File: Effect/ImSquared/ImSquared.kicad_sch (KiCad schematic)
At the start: 55 parts, among them J1 Conn_01x04_Pin, J2 Conn_01x03_Pin, Q1 DMMT5551, Q2 DMMT5551, Q3 DMMT5551, Q4 DMMT5551, U1 OPA1656, U2 OPA1656, U3 OPA1656

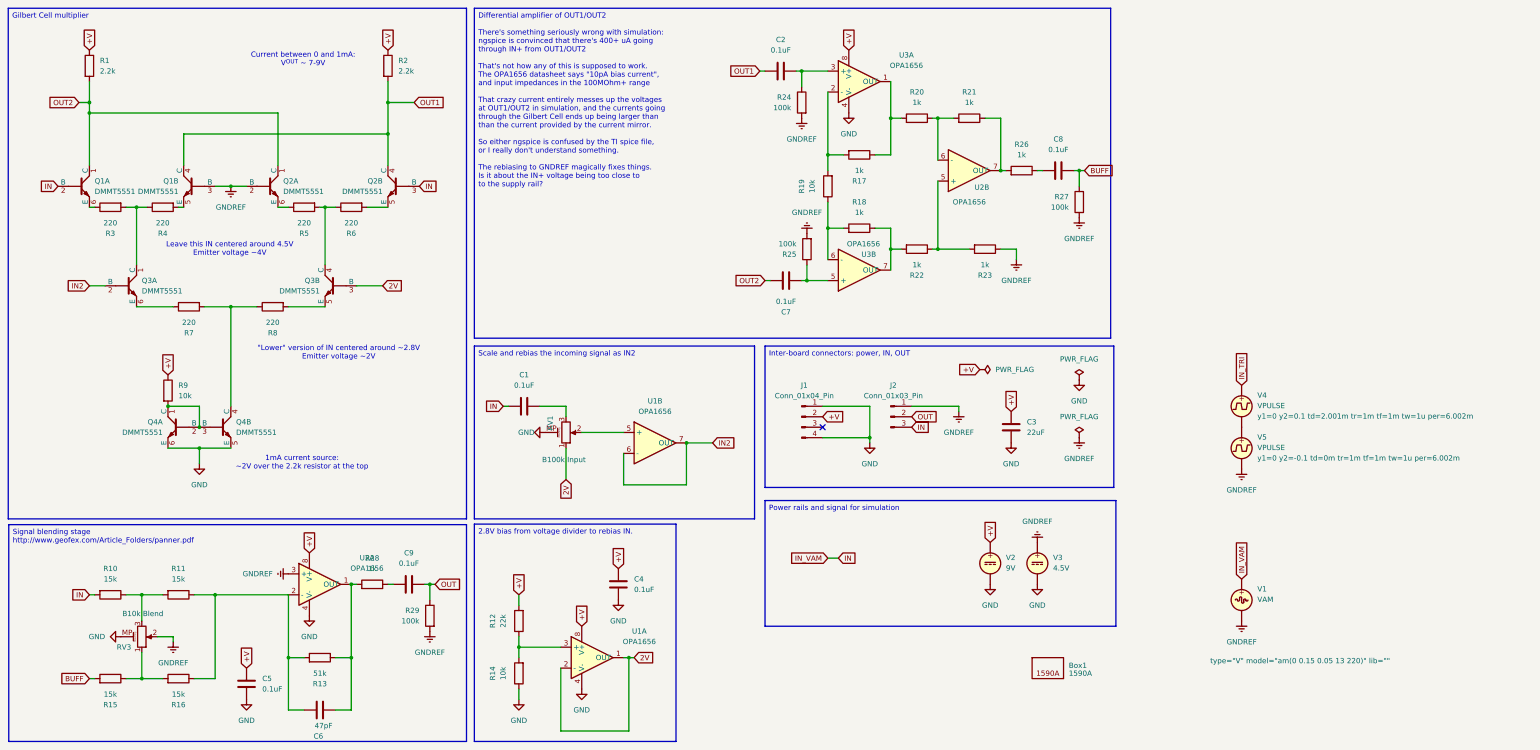
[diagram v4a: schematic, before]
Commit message: Try simulating an actual wav file input with new locally-built tooling
So this "works" in the sense that I built local copies of ngspice and
kicad and now it supports wav file input and output to simulation, and I
am trying to use some sample files to simulate what the heck it does and
sounds like.

That didn't work very well because the linear interpolation of samples
in the experimental ngspice wav branch seems quite broken, causing the
input signal to be more of a discrete staircase signal.

Which in turn then caused pretty much immediate "Timestep too small"
errors for the simulation because it's much too sensitive to not
converging, and the stepwise voltage jumps seemed to make an already
fragile situation much much worse.

I have a local hack for that ngspice sample interpolation issue that
makes the simulation mostly work, in that now I see the result on the
real signal.  I can make it even generate a result wav-file, but only if
I end up removing a lot of the surrounding circuitry, because ngspice
still ends up crapping out eventually even with my linearization fixlet.

The goal? See why the effect seems to simply not work very well on bass
guitar (although I have a suspicion that it's just the fact that the
rest of the sound path ends up filtering everything up and cleaning up
the fuzz).

I do suspect that the whole "use squaring as a octaver fuzz" is a
completely broken concept to begin with, but setting things up to use a
real signal is still a good idea.

Signed-off-by: Linus Torvalds <torvalds@linux-foundation.org>
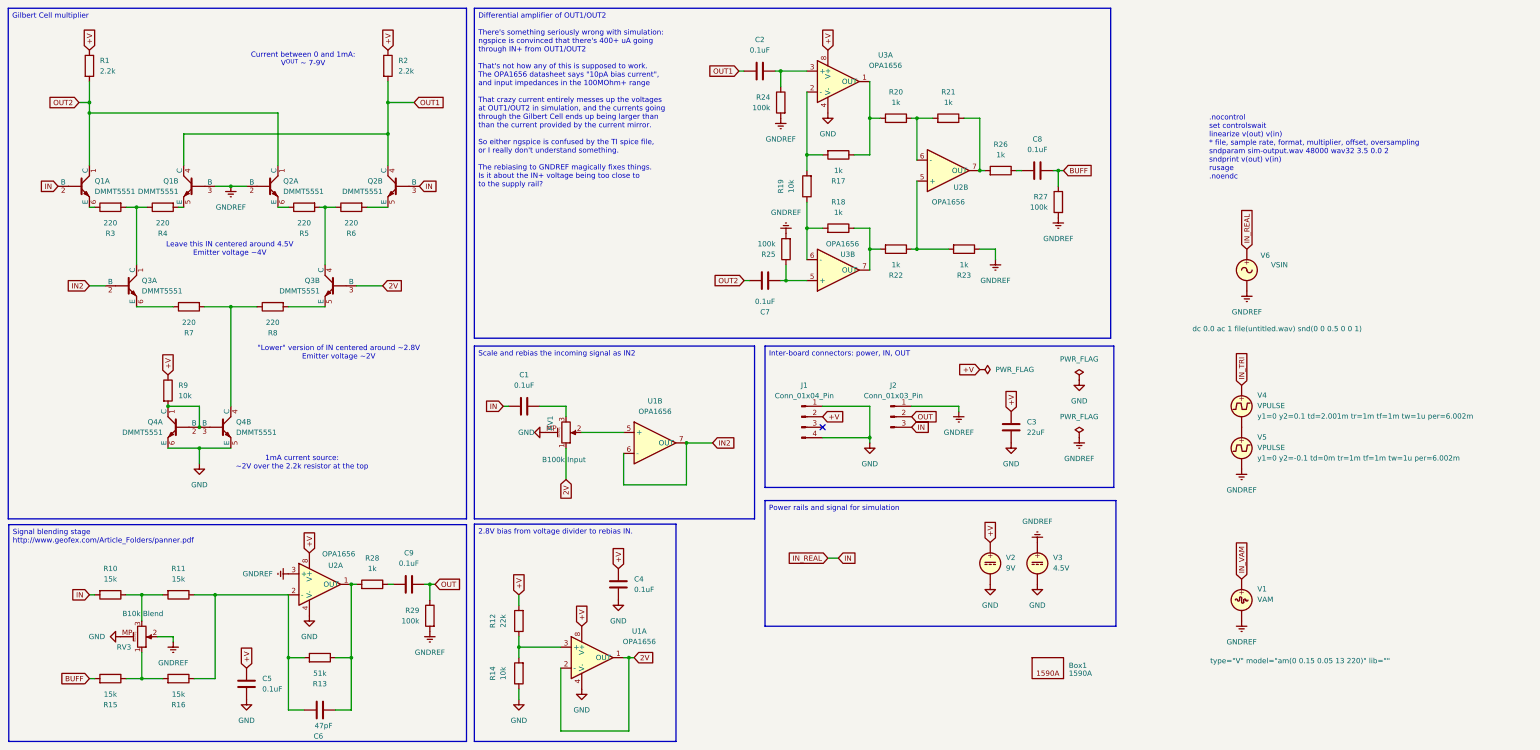
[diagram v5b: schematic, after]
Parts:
- added V6: VSIN, symbol Simulation_SPICE:VSIN
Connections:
- net GNDREF: now also V6.2
- net IN: now also V6.1; no longer V1.1
- new net IN_VAM: V1.1
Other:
- note added: ".nocontrol set controlswait linearize v(out) v(in) * file, sample rate, format, multiplier, offset, oversampling sndparam sim-output.wav 48000 wav32 3.5 0.0 2 sndprint v(out) v(in) rusage .noendc"
- moved on the sheet: C2, C7, C8, R17, R18, R19, R20, R21, R22, R23, R24, R25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

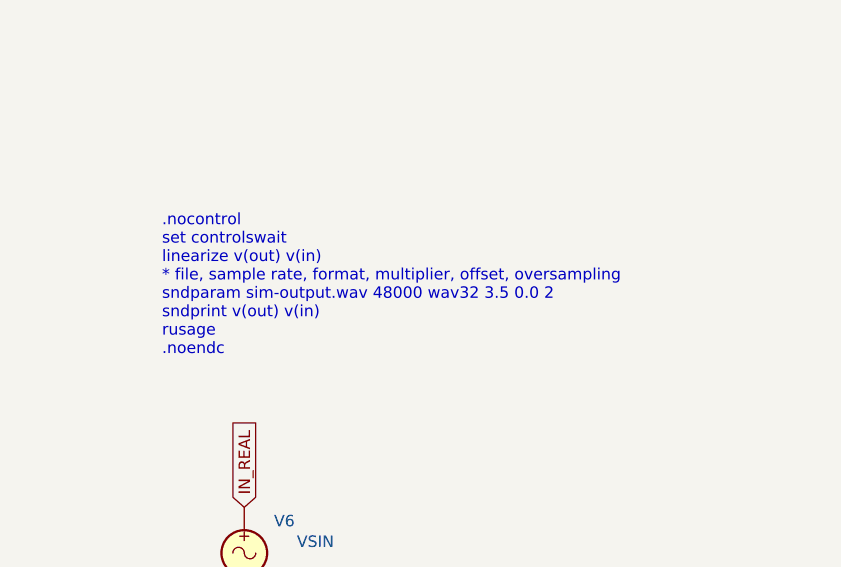
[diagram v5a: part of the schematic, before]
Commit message: Re-enable writing simulation result output wav file
Based on some hints from Holger Vogt I actually got the whole ImSquared
circuit to simulate for a full five-second sound simulation.  So now I
can hear it sounding bad without actually having hardware back.

So this enables the writeback of the sim-output.wav file, and uses the
offset parameter to get a proper signal output even at GNDREF instead of
having to re-bias the output to real ground in the circuit itself.

[ NOTE NOTE NOTE: I wasted more time than I'd like to admit on this due
  to interactions between kicad and ngspice.

  In particular, changing the parameters in the kicad text fields
  requires you to just quit and restart the whole thing for things to
  actually take effect.

  That was very confusing with me making changes to the parameters that
  didn't take effect. I'm sure I'll forget about this once more, so
  adding a big note to myself here about it. ]

It really doesn't sound great, but the circuit works, and simulation now
works too (but still needs my ngspice patch for input sample
interpolation).

The whole signal squaring approach does actually seem to work as a
octaver fuzz, but it's obviously a lot more sensitive to the input
voltage range than a plain precision rectification circuit is.

With the rectifier circuit, the output amplitude has a simple linear
relationship with the input signal, while the squaring function is
obviously non-linear.

It still might be an advantage once you mix in the original signal, with
a quiet signal giving much less distortion than a loud one.  But based
on limited testing, it ends up being pretty finicky so that "advantage"
is rather questionable.

Still, this exercise has taught me something new.  Both on the circuit
side and about ngspice.

Signed-off-by: Linus Torvalds <torvalds@linux-foundation.org>
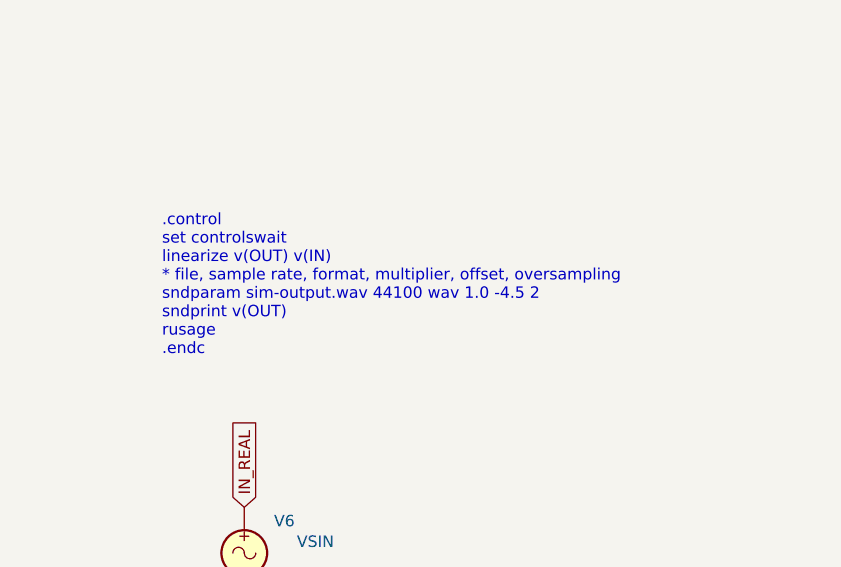
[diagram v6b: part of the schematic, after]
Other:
- note added: ".control set controlswait linearize v(OUT) v(IN) * file, sample rate, format, multiplier, offset, oversampling sndparam sim-output.wav 44100 wav 1.0 -4.5 2 sndprint v(OUT) rusage .endc"
- note removed: ".nocontrol set controlswait linearize v(out) v(in) * file, sample rate, format, multiplier, offset, oversampling sndparam sim-output.wav 48000 wav32 3.5 0.0 2 sndprint v(out) v(in) rusage .noendc"
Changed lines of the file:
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@@
 		)
 	)
-	(text ".nocontrol\nset controlswait\nlinearize v(out) v(in)\n* file, sample rate, format, multiplier, offset, oversampling\nsndparam sim-output.wav 48000 wav32 3.5 0.0 2\nsndprint v(out) v(in)\nrusage\n.noendc\n"
+	(text ".control\nset controlswait\nlinearize v(OUT) v(IN)\n* file, sample rate, format, multiplier, offset, oversampling\nsndparam sim-output.wav 44100 wav 1.0 -4.5 2\nsndprint v(OUT)\nrusage\n.endc\n"
 		(exclude_from_sim no)
 		(at 304.546 47.752 0)
@@
 	)
 	(symbol
-		(lib_id "power:GNDREF")
-		(at 115.57 165.1 0)
-		(unit 1)
-		(exclude_from_sim no)
-		(in_bom yes)
-		(on_board yes)
-		(dnp no)
-		(fields_autoplaced yes)
-		(property "Reference" "#PWR027"
-			(at 115.57 171.45 0)
-			(hide yes)
-			(effects
-				(font
-					(size 1.27 1.27)
-				)
-			)
-		)
-		(property "Value" "GNDREF"
-			(at 115.57 170.18 0)
-			(effects
-				(font
-					(size 1.27 1.27)
-				)
-			)
-		)
-		(property "Footprint" ""
-			(at 115.57 165.1 0)
-			(hide yes)
-			(effects
-				(font
-					(size 1.27 1.27)
-				)
-			)
-		)
-		(property "Datasheet" ""
-			(at 115.57 165.1 0)
-			(hide yes)
-			(effects
-				(font
-					(size 1.27 1.27)
-				)
-			)
-		)
-		(property "Description" "Power symbol creates a global label with name \"GNDREF\" , reference supply ground"
-			(at 115.57 165.1 0)
-			(hide yes)
-			(effects
-				(font
-					(size 1.27 1.27)
-				)
-			)
-		)
-		(pin "1"
-		)
-		(instances
-			(project "ImSquared"
-				(path "/9e337e0b-885b-4d2b-99a2-62cdd082c615"
-					(reference "#PWR027")
-					(unit 1)
-				)
-			)
-		)
-	)
-	(symbol
 		(lib_id "Device:R_Potentiometer_MountingPin")
 		(at 45.72 166.37 0)
@@
 					(unit 1)
 				)
+			)
+		)
+	)
+	(symbol
+		(lib_id "power:GNDREF")
+		(at 115.57 165.1 0)
+		(unit 1)
+		(exclude_from_sim no)
+		(in_bom yes)
+		(on_board yes)
+		(dnp no)
+		(fields_autoplaced yes)
+		(property "Reference" "#PWR027"
+			(at 115.57 171.45 0)
+			(hide yes)
+			(effects
+				(font
+					(size 1.27 1.27)
+				)
+			)
+		)
+		(property "Value" "GNDREF"
+			(at 115.57 170.18 0)
+			(effects
+				(font
+					(size 1.27 1.27)
+				)
+			)
+		)
+		(property "Footprint" ""
+			(at 115.57 165.1 0)
+			(hide yes)
+			(effects
+				(font
+					(size 1.27 1.27)
+				)
+			)
+		)
+		(property "Datasheet" ""
+			(at 115.57 165.1 0)
+			(hide yes)
+			(effects
+				(font
+					(size 1.27 1.27)
+				)
+			)
+		)
+		(property "Description" "Power symbol creates a global label with name \"GNDREF\" , reference supply ground"
+			(at 115.57 165.1 0)
+			(hide yes)
+			(effects
+				(font
+					(size 1.27 1.27)
+				)
+			)
+		)
+		(pin "1"
+		)
+		(instances
+			(project "ImSquared"
+				(path "/9e337e0b-885b-4d2b-99a2-62cdd082c615"
+					(reference "#PWR027")
+					(unit 1)
+				)
